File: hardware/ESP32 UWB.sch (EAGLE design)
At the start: 55 parts, among them J2 HEADER-12P-2.54, J3 10118194-0001LF, Q1 S8050, Q2 S8050, SW1 BUTTON, SW2 BUTTON, U1 AMS1117-3.3, U2 ESP32-C3-MINI-1-N4, U3 SILICON_LABS_CP2102N-A01-GQFN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, U4 DWM1000

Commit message: replaced footprint of C7
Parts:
- C7: value 100nf -> 100n; device microbuilder:CAP_CERAMIC0603_NO -> isystems:CAP_CERAMIC0603
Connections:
- net GND: now also C7.P$2; no longer C7.2
- net RESET: now also C7.P$1; no longer C7.1
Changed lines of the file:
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@@
 <part name="R4" library="isystems" deviceset="RESISTOR" device="0603" value="10K"/>
 <part name="R3" library="isystems" deviceset="RESISTOR" device="0603" value="10K"/>
-<part name="C7" library="microbuilder" deviceset="CAP_CERAMIC" device="0603_NO" value="100nf"/>
 <part name="R1" library="isystems" deviceset="RESISTOR" device="0603" value="470R"/>
 <part name="R5" library="isystems" deviceset="RESISTOR" device="0603" value="1K"/>
@@
 <part name="GND5" library="supply1" deviceset="GND" device=""/>
 <part name="SJ1" library="isystems" deviceset="SJ" device="S"/>
+<part name="C7" library="isystems" deviceset="CAP_CERAMIC" device="0603" value="100n"/>
 </parts>
 <sheets>
@@
 <attribute name="VALUE" x="234.696" y="36.068" size="1.27" layer="96" ratio="10" rot="R270"/>
 </instance>
-<instance part="C7" gate="G$1" x="233.68" y="20.32"/>
 <instance part="R1" gate="G$1" x="193.04" y="36.83" smashed="yes" rot="R90">
 <attribute name="NAME" x="191.897" y="37.846" size="1.27" layer="95" ratio="10" rot="R180"/>
@@
 <instance part="GND5" gate="1" x="358.14" y="99.06"/>
 <instance part="SJ1" gate="1" x="289.56" y="154.94"/>
+<instance part="C7" gate="G$1" x="233.68" y="20.32"/>
 </instances>
 <busses>
@@
 <label x="234.188" y="13.97" size="1.27" layer="95" ratio="10"/>
 <pinref part="GND23" gate="1" pin="GND"/>
-<pinref part="C7" gate="G$1" pin="2"/>
+<pinref part="C7" gate="G$1" pin="P$2"/>
 </segment>
 <segment>
@@
 <segment>
 <pinref part="R3" gate="G$1" pin="1"/>
-<pinref part="C7" gate="G$1" pin="1"/>
 <wire x1="233.68" y1="29.21" x2="233.68" y2="27.94" width="0.1524" layer="91"/>
 <wire x1="233.68" y1="27.94" x2="233.68" y2="25.4" width="0.1524" layer="91"/>
@@
 <label x="251.46" y="27.94" size="1.016" layer="95" xref="yes"/>
 <junction x="233.68" y="27.94"/>
-</segment>
-<segment>
+<pinref part="C7" gate="G$1" pin="P$1"/>
+</segment>
+<segment>

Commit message: updated library
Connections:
- net +3V3: now also C10.1, C11.1, C12.1, C4.1, C5.1, C6.1, C8.1, C9.1; no longer C10.P$1, C11.P$1, C12.P$1, C4.P$1, C5.P$1, C6.P$1, C8.P$1, C9.P$1
- net GND: now also C1.2, C10.2, C11.2, C12.2, C2.2, C3.2, C4.2, C5.2, C6.2, C7.2, C8.2, C9.2; no longer C1.P$2, C10.P$2, C11.P$2, C12.P$2, C2.P$2, C3.P$2, C4.P$2, C5.P$2, C6.P$2, C7.P$2, C8.P$2, C9.P$2
- net RESET: now also C7.1; no longer C7.P$1
- net VBUS: now also C1.1, C2.1; no longer C1.P$1, C2.P$1
- net VDD5V: now also C3.1; no longer C3.P$1
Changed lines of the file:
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@@
 <label x="234.188" y="13.97" size="1.27" layer="95" ratio="10"/>
 <pinref part="GND23" gate="1" pin="GND"/>
-<pinref part="C7" gate="G$1" pin="P$2"/>
+<pinref part="C7" gate="G$1" pin="2"/>
 </segment>
 <segment>
@@
 <wire x1="236.22" y1="96.52" x2="226.06" y2="96.52" width="0.1524" layer="91"/>
 <junction x="226.06" y="96.52"/>
-<pinref part="C8" gate="G$1" pin="P$2"/>
-<pinref part="C6" gate="G$1" pin="P$2"/>
+<pinref part="C8" gate="G$1" pin="2"/>
+<pinref part="C6" gate="G$1" pin="2"/>
 </segment>
 <segment>
@@
 <segment>
 <pinref part="GND19" gate="1" pin="GND"/>
-<pinref part="C10" gate="G$1" pin="P$2"/>
+<pinref part="C10" gate="G$1" pin="2"/>
 <wire x1="330.2" y1="33.02" x2="330.2" y2="30.48" width="0.1524" layer="91"/>
-<pinref part="C11" gate="G$1" pin="P$2"/>
+<pinref part="C11" gate="G$1" pin="2"/>
 <wire x1="330.2" y1="30.48" x2="330.2" y2="27.94" width="0.1524" layer="91"/>
 <wire x1="337.82" y1="33.02" x2="337.82" y2="30.48" width="0.1524" layer="91"/>
@@
 <segment>
 <pinref part="GND2" gate="1" pin="GND"/>
-<pinref part="C9" gate="G$1" pin="P$2"/>
+<pinref part="C9" gate="G$1" pin="2"/>
 <wire x1="325.12" y1="124.46" x2="325.12" y2="127" width="0.1524" layer="91"/>
 <wire x1="325.12" y1="127" x2="325.12" y2="129.54" width="0.1524" layer="91"/>
 <junction x="325.12" y="127"/>
 <wire x1="340.36" y1="127" x2="325.12" y2="127" width="0.1524" layer="91"/>
-<pinref part="C12" gate="G$1" pin="P$2"/>
+<pinref part="C12" gate="G$1" pin="2"/>
 <wire x1="340.36" y1="129.54" x2="340.36" y2="127" width="0.1524" layer="91"/>
 </segment>
@@
 <segment>
 <pinref part="GND14" gate="1" pin="GND"/>
-<pinref part="C4" gate="G$1" pin="P$2"/>
+<pinref part="C4" gate="G$1" pin="2"/>
 <wire x1="198.12" y1="144.78" x2="198.12" y2="142.24" width="0.1524" layer="91"/>
-<pinref part="C5" gate="G$1" pin="P$2"/>
+<pinref part="C5" gate="G$1" pin="2"/>
 <wire x1="198.12" y1="142.24" x2="198.12" y2="139.7" width="0.1524" layer="91"/>
 <wire x1="205.74" y1="144.78" x2="205.74" y2="142.24" width="0.1524" layer="91"/>
@@
 </segment>
 <segment>
-<pinref part="C3" gate="G$1" pin="P$2"/>
+<pinref part="C3" gate="G$1" pin="2"/>
 <pinref part="GND17" gate="1" pin="GND"/>
 <wire x1="160.02" y1="147.32" x2="160.02" y2="139.7" width="0.1524" layer="91"/>
@@
 <segment>
 <pinref part="GND18" gate="1" pin="GND"/>
-<pinref part="C1" gate="G$1" pin="P$2"/>
+<pinref part="C1" gate="G$1" pin="2"/>
 <wire x1="119.38" y1="147.32" x2="119.38" y2="144.78" width="0.1524" layer="91"/>
-<pinref part="C2" gate="G$1" pin="P$2"/>
+<pinref part="C2" gate="G$1" pin="2"/>
 <wire x1="119.38" y1="144.78" x2="119.38" y2="139.7" width="0.1524" layer="91"/>
 <wire x1="129.54" y1="147.32" x2="129.54" y2="144.78" width="0.1524" layer="91"/>
@@
 <pinref part="U1" gate="G$1" pin="OUT"/>
 <wire x1="198.12" y1="157.48" x2="177.8" y2="157.48" width="0.1524" layer="91"/>
-<pinref part="C4" gate="G$1" pin="P$1"/>
+<pinref part="C4" gate="G$1" pin="1"/>
 <wire x1="198.12" y1="152.4" x2="198.12" y2="157.48" width="0.1524" layer="91"/>
-<pinref part="C5" gate="G$1" pin="P$1"/>
+<pinref part="C5" gate="G$1" pin="1"/>
 <wire x1="205.74" y1="152.4" x2="205.74" y2="157.48" width="0.1524" layer="91"/>
 <wire x1="205.74" y1="157.48" x2="198.12" y2="157.48" width="0.1524" layer="91"/>
@@
 <junction x="330.2" y="44.45"/>
 <wire x1="330.2" y1="40.64" x2="330.2" y2="44.45" width="0.1524" layer="91"/>
-<pinref part="C10" gate="G$1" pin="P$1"/>
-<pinref part="C11" gate="G$1" pin="P$1"/>
+<pinref part="C10" gate="G$1" pin="1"/>
+<pinref part="C11" gate="G$1" pin="1"/>
 <wire x1="337.82" y1="40.64" x2="337.82" y2="44.45" width="0.1524" layer="91"/>
 <junction x="337.82" y="44.45"/>
@@
 <junction x="226.06" y="109.22"/>
 <wire x1="236.22" y1="109.22" x2="236.22" y2="106.68" width="0.1524" layer="91"/>
-<pinref part="C8" gate="G$1" pin="P$1"/>
-<pinref part="C6" gate="G$1" pin="P$1"/>
+<pinref part="C8" gate="G$1" pin="1"/>
+<pinref part="C6" gate="G$1" pin="1"/>
 </segment>
 <segment>
@@
 </segment>
 <segment>
-<pinref part="C9" gate="G$1" pin="P$1"/>
+<pinref part="C9" gate="G$1" pin="1"/>
 <wire x1="325.12" y1="137.16" x2="325.12" y2="139.7" width="0.1524" layer="91"/>
 <wire x1="325.12" y1="139.7" x2="340.36" y2="139.7" width="0.1524" layer="91"/>
@@
 <wire x1="325.12" y1="139.7" x2="325.12" y2="144.78" width="0.1524" layer="91"/>
 <junction x="325.12" y="139.7"/>
-<pinref part="C12" gate="G$1" pin="P$1"/>
+<pinref part="C12" gate="G$1" pin="1"/>
 <wire x1="340.36" y1="137.16" x2="340.36" y2="139.7" width="0.1524" layer="91"/>
 </segment>
@@
 <wire x1="119.38" y1="157.48" x2="119.38" y2="162.56" width="0.1524" layer="91"/>
 <pinref part="U$4" gate="G$1" pin="VBUS"/>
-<pinref part="C1" gate="G$1" pin="P$1"/>
+<pinref part="C1" gate="G$1" pin="1"/>
 <wire x1="119.38" y1="154.94" x2="119.38" y2="157.48" width="0.1524" layer="91"/>
 <junction x="119.38" y="157.48"/>
-<pinref part="C2" gate="G$1" pin="P$1"/>
+<pinref part="C2" gate="G$1" pin="1"/>
 <wire x1="129.54" y1="154.94" x2="129.54" y2="157.48" width="0.1524" layer="91"/>
 <junction x="129.54" y="157.48"/>
@@
 <label x="251.46" y="27.94" size="1.016" layer="95" xref="yes"/>
 <junction x="233.68" y="27.94"/>
-<pinref part="C7" gate="G$1" pin="P$1"/>
+<pinref part="C7" gate="G$1" pin="1"/>
 </segment>
 <segment>
@@
 <wire x1="160.02" y1="157.48" x2="144.78" y2="157.48" width="0.1524" layer="91"/>
 <pinref part="U1" gate="G$1" pin="IN"/>
-<pinref part="C3" gate="G$1" pin="P$1"/>
+<pinref part="C3" gate="G$1" pin="1"/>
 <wire x1="160.02" y1="157.48" x2="162.56" y2="157.48" width="0.1524" layer="91"/>
 <wire x1="160.02" y1="154.94" x2="160.02" y2="157.48" width="0.1524" layer="91"/>

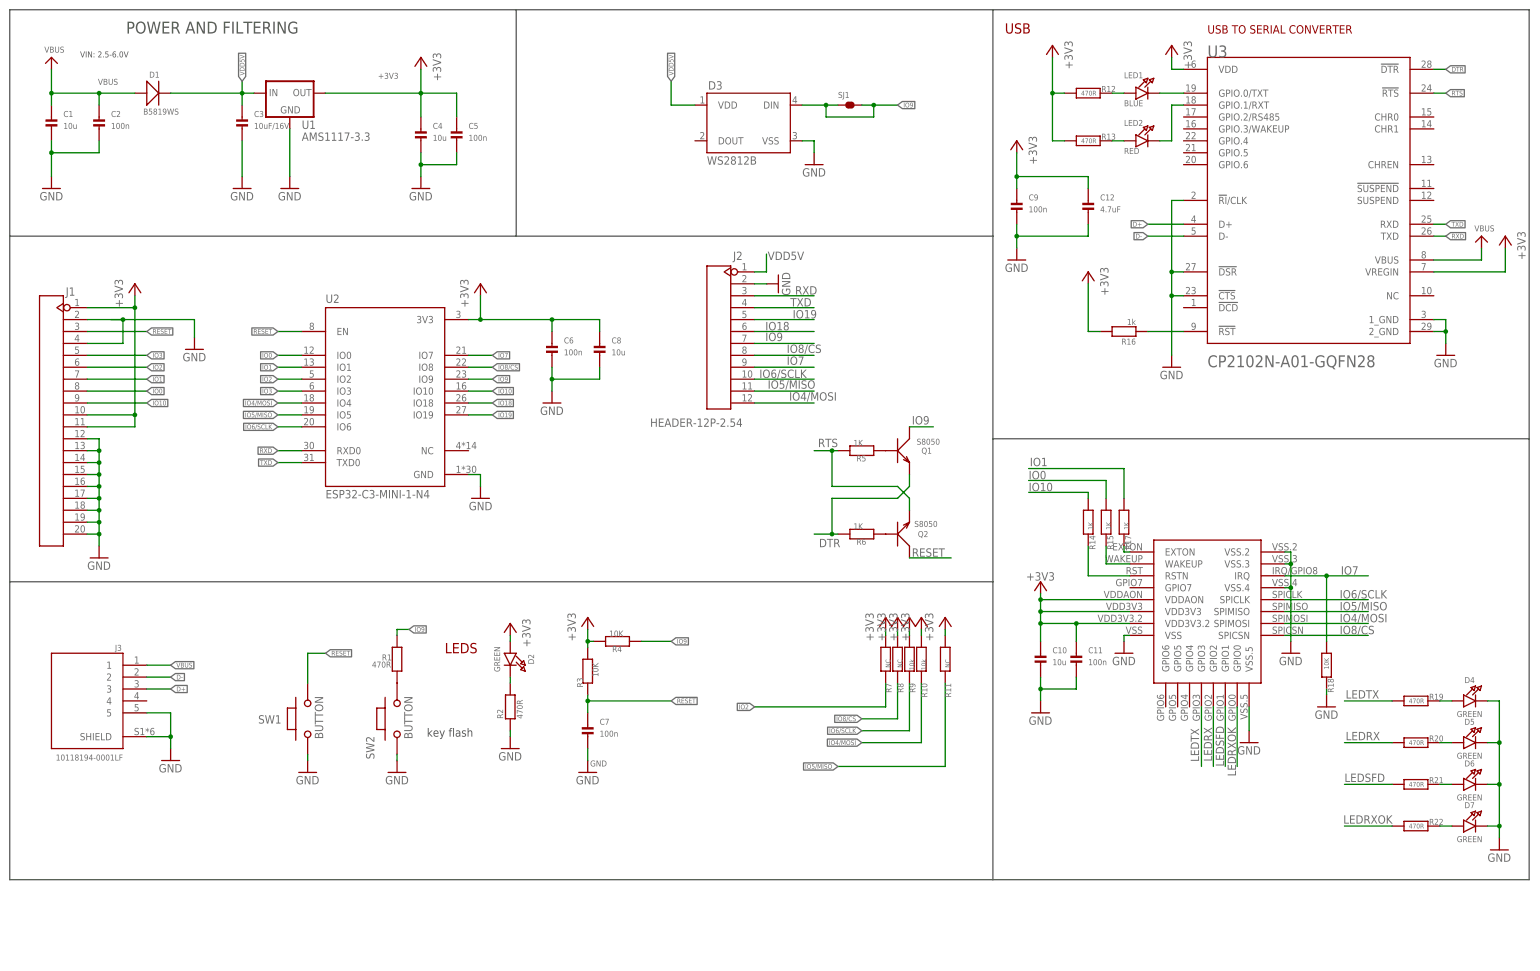
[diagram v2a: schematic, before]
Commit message: replaced WS2812 with SK6812-mini-e
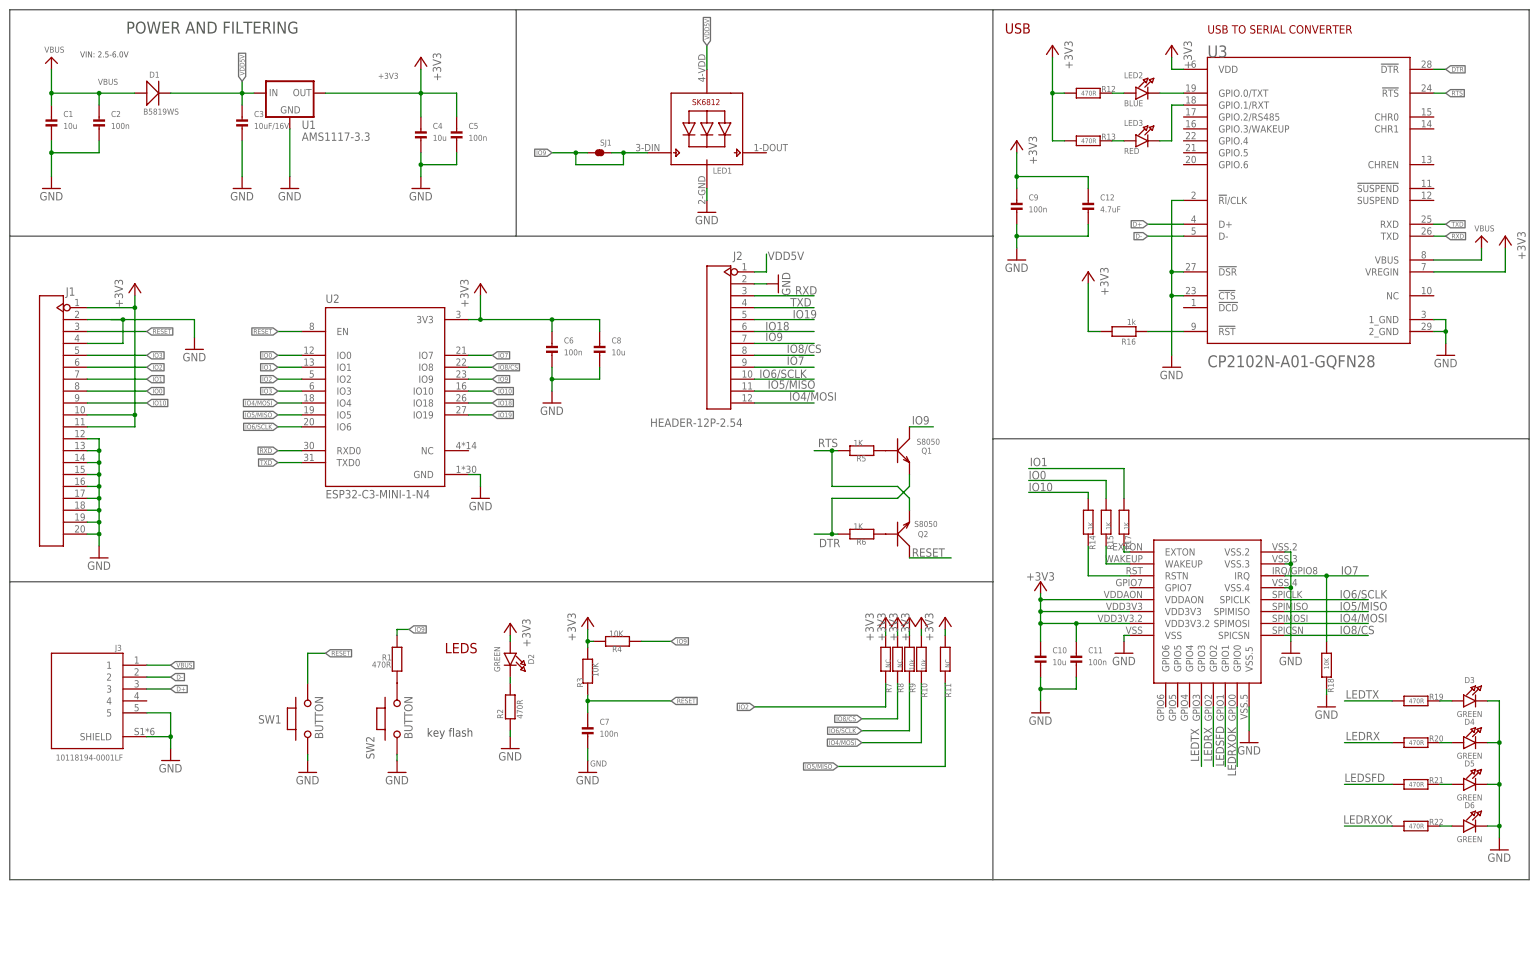
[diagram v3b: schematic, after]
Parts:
- removed D7: GREEN, microbuilder:LED0805_NOOUTLINE
- added LED3: RED, isystems:LED0603_NOOUTLINE
- D3: value WS2812B -> GREEN; device SparkFun-LED:WS2812B -> microbuilder:LED0805_NOOUTLINE
- LED1: value BLUE -> (none); device isystems:LED0603_NOOUTLINE -> SK6812:SK6812_3535
- LED2: value RED -> BLUE
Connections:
- net GND: now also D3.C, LED1.GND; no longer D3.VSS, D7.C
- net IO9: now also LED1.DI; no longer D3.DIN
- net N$1: now also D3.A; no longer D4.A
- net N$16: now also D4.A; no longer D5.A
- net N$17: now also D5.A; no longer D6.A
- net N$18: now also D6.A; no longer D7.A
- net N$2: now also LED2.A; no longer LED1.A
- net N$3: now also LED2.C; no longer LED1.C
- net N$4: now also LED3.A; no longer LED2.A
- net N$6: now also LED3.C; no longer LED2.C
- net VDD5V: now also LED1.VDD; no longer D3.VDD
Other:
- moved on the sheet: D4, D5, D6, LED2, SJ1

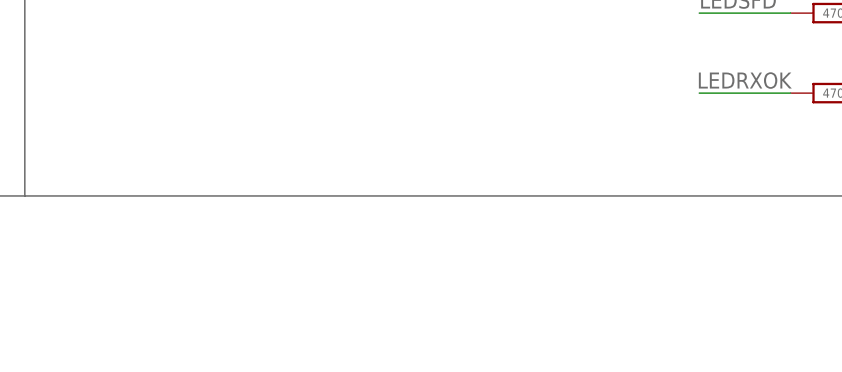
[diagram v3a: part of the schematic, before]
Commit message: added assembly variant without USB serial converter
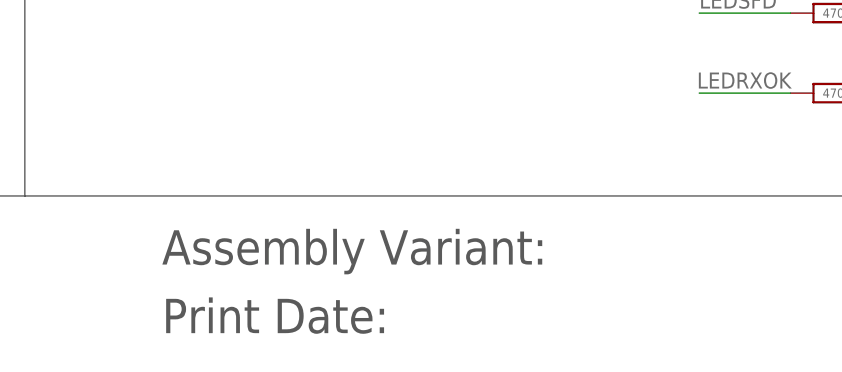
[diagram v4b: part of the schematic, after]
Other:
- note added: "Assembly Variant:"
- note added: "Print Date:"
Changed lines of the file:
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@@
 </attributes>
 <variantdefs>
+<variantdef name="No USB"/>
+<variantdef name="Normal" current="yes"/>
 </variantdefs>
 <classes>
@@
 <part name="+3V13" library="supply1" deviceset="+3V3" device=""/>
 <part name="+3V14" library="supply1" deviceset="+3V3" device=""/>
-<part name="Q2" library="Discrete" deviceset="TRANSISTOR-NPN*" device="-SOT23" value="S8050"/>
-<part name="Q1" library="Discrete" deviceset="TRANSISTOR-NPN*" device="-SOT23" value="S8050"/>
+<part name="Q2" library="Discrete" deviceset="TRANSISTOR-NPN*" device="-SOT23" value="S8050">
+<variant name="No USB" populate="no"/>
+</part>
+<part name="Q1" library="Discrete" deviceset="TRANSISTOR-NPN*" device="-SOT23" value="S8050">
+<variant name="No USB" populate="no"/>
+</part>
 <part name="D1" library="Discrete" deviceset="D*" device="'0805'" value="B5819WS"/>
 <part name="GND8" library="supply1" deviceset="GND" device=""/>
@@
 <part name="R3" library="isystems" deviceset="RESISTOR" device="0603" value="10K"/>
 <part name="R1" library="isystems" deviceset="RESISTOR" device="0603" value="470R"/>
-<part name="R5" library="isystems" deviceset="RESISTOR" device="0603" value="1K"/>
-<part name="R6" library="isystems" deviceset="RESISTOR" device="0603" value="1K"/>
+<part name="R5" library="isystems" deviceset="RESISTOR" device="0603" value="1K">
+<variant name="No USB" populate="no"/>
+</part>
+<part name="R6" library="isystems" deviceset="RESISTOR" device="0603" value="1K">
+<variant name="No USB" populate="no"/>
+</part>
 <part name="J1" library="Connector" deviceset="HEADER-20P" device="-2.54"/>
 <part name="J2" library="Connector" deviceset="HEADER-12P" device="-2.54"/>
@@
 <part name="+3V8" library="supply1" deviceset="+3V3" device=""/>
 <part name="GND1" library="supply1" deviceset="GND" device=""/>
-<part name="U3" library="Silicon Labs - CP2102N-A01-GQFN28" deviceset="SILICON_LABS_CP2102N-A01-GQFN28" device="SILICON_LABS_CP2102N-A01-GQFN28_0_3" value="SILICON_LABS_CP2102N-A01-GQFN28SILICON_LABS_CP2102N-A01-GQFN28_0_3"/>
+<part name="U3" library="Silicon Labs - CP2102N-A01-GQFN28" deviceset="SILICON_LABS_CP2102N-A01-GQFN28" device="SILICON_LABS_CP2102N-A01-GQFN28_0_3" value="SILICON_LABS_CP2102N-A01-GQFN28SILICON_LABS_CP2102N-A01-GQFN28_0_3">
+<variant name="No USB" populate="no"/>
+</part>
 <part name="GND3" library="supply1" deviceset="GND" device=""/>
 <part name="U$8" library="microbuilder" deviceset="VBUS" device=""/>
-<part name="R12" library="isystems" deviceset="RESISTOR" device="0603" value="470R"/>
-<part name="LED2" library="isystems" deviceset="LED" device="0603_NOOUTLINE" value="BLUE"/>
-<part name="R13" library="isystems" deviceset="RESISTOR" device="0603" value="470R"/>
-<part name="LED3" library="isystems" deviceset="LED" device="0603_NOOUTLINE" value="RED"/>
+<part name="R12" library="isystems" deviceset="RESISTOR" device="0603" value="470R">
+<variant name="No USB" populate="no"/>
+</part>
+<part name="LED2" library="isystems" deviceset="LED" device="0603_NOOUTLINE" value="BLUE">
+<variant name="No USB" populate="no"/>
+</part>
+<part name="R13" library="isystems" deviceset="RESISTOR" device="0603" value="470R">
+<variant name="No USB" populate="no"/>
+</part>
+<part name="LED3" library="isystems" deviceset="LED" device="0603_NOOUTLINE" value="RED">
+<variant name="No USB" populate="no"/>
+</part>
 <part name="U1" library="SparkFun-PowerIC" deviceset="V_REG_MIC2920" device="" value="AMS1117-3.3"/>
 <part name="+3V3" library="supply1" deviceset="+3V3" device=""/>
 <part name="+3V10" library="supply1" deviceset="+3V3" device=""/>
 <part name="+3V15" library="supply1" deviceset="+3V3" device=""/>
-<part name="C9" library="isystems" deviceset="CAP_CERAMIC" device="0603" value="100n"/>
-<part name="C12" library="isystems" deviceset="CAP_CERAMIC" device="0603" value="4.7uF"/>
+<part name="C9" library="isystems" deviceset="CAP_CERAMIC" device="0603" value="100n">
+<variant name="No USB" populate="no"/>
+</part>
+<part name="C12" library="isystems" deviceset="CAP_CERAMIC" device="0603" value="4.7uF">
+<variant name="No USB" populate="no"/>
+</part>
 <part name="+3V17" library="supply1" deviceset="+3V3" device=""/>
 <part name="GND2" library="SparkFun-Aesthetics" deviceset="GND" device=""/>
@@
 <part name="GND6" library="supply1" deviceset="GND" device=""/>
 <part name="GND12" library="supply1" deviceset="GND" device=""/>
-<part name="R16" library="isystems" deviceset="RESISTOR" device="0603" value="1k"/>
+<part name="R16" library="isystems" deviceset="RESISTOR" device="0603" value="1k">
+<variant name="No USB" populate="no"/>
+</part>
 <part name="+3V12" library="supply1" deviceset="+3V3" device=""/>
 <part name="C8" library="isystems" deviceset="CAP_CERAMIC" device="0603" value="10u"/>
@@
 <wire x1="218.44" y1="127" x2="320.04" y2="127" width="0.1524" layer="97"/>
 <wire x1="218.44" y1="175.26" x2="218.44" y2="127" width="0.1524" layer="97"/>
+<text x="391.16" y="-17.78" size="3.81" layer="97" ratio="12">&gt;ASSEMBLY_VARIANT</text>
+<text x="335.28" y="-17.78" size="3.81" layer="97" ratio="13">Assembly Variant:</text>
+<text x="335.28" y="-25.4" size="3.81" layer="97" ratio="13">Print Date:</text>
+<text x="370.84" y="-25.4" size="3.81" layer="97" ratio="12">&gt;PLOT_DATE_TIME</text>
 </plain>
 <instances>
